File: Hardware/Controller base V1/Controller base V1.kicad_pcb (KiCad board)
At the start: 2 copper layers, 30 x 50 mm, 29 parts, among them J1 USB_C_Receptacle_USB2.0_16P, J7 Conn_02x10_Counter_Clockwise, J8 Conn_02x10_Counter_Clockwise, SW4 SW_Push, U1 AZ1117CH-3.3TRG1, U2 ESP32-S3-WROOM-1U-N4

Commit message: update
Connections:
- J8 pad 16: GND -> GPIO39
- J8 pad 18: GND -> GPIO40
- U2 pad 32: unconnected-(U2-IO39-Pad32) -> GPIO39
- U2 pad 33: unconnected-(U2-IO40-Pad33) -> GPIO40
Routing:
- net GPIO40: track 0.00 -> 15.6 mm, vias 0 -> 1
- net GPIO39: track 0.00 -> 13.3 mm, vias 0 -> 1
- net GND: track 75.0 -> 69.2 mm
- net GPIO16: track 12.8 -> 14.0 mm
- net GPIO15: track 16.2 -> 15.2 mm
- net GPIO6: track 12.1 -> 12.7 mm
- net GPIO5: track 13.4 -> 13.9 mm

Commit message: added test points
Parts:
- added 3V3: TestPoint, MCU_Controller:TestPoint_Pad_D1.0mm, F.Cu at (135.8, 77.1)
- added Gnd1: TestPoint, MCU_Controller:TestPoint_Pad_D1.0mm, F.Cu at (132.0, 108.8)
- added VBUS: TestPoint, MCU_Controller:TestPoint_Pad_D1.0mm, F.Cu at (149.3, 73.5)
- renumbered TP4 to D+1, TP3 to D-1, J7 to J3, J8 to J4, TP1 to RX0, SW4 to SW1, TP2 to TX0
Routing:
- net GND: track 69.2 -> 81.4 mm
- net VBUS: track 24.4 -> 27.7 mm
- net VCC_3V3: track 59.5 -> 62.2 mm

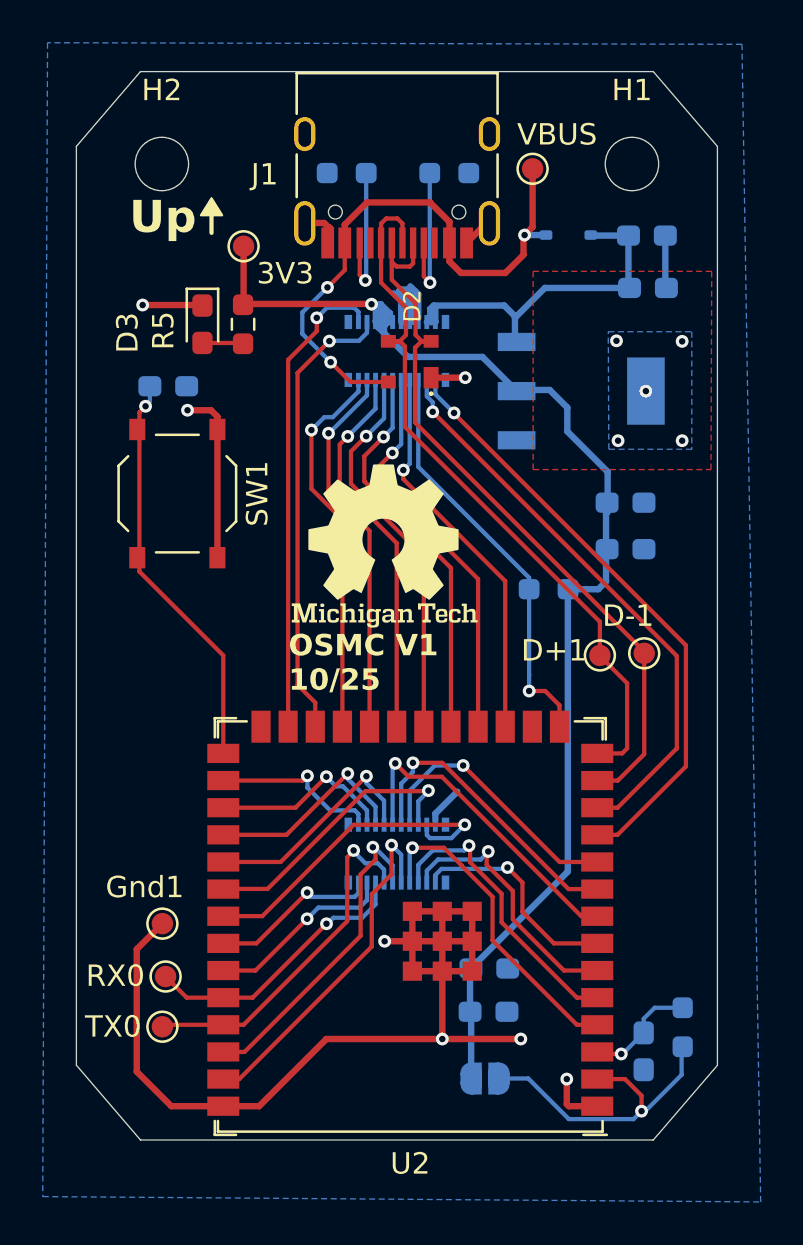
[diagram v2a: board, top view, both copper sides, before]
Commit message: trace update
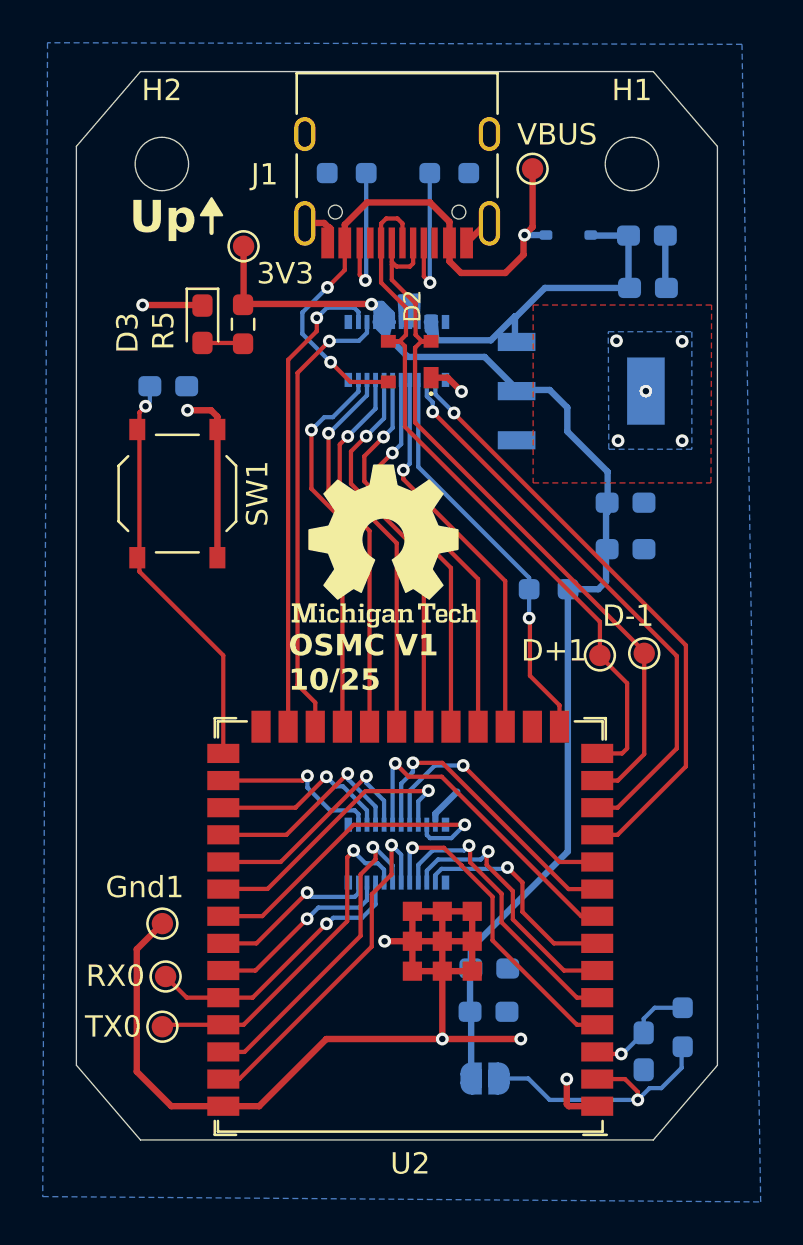
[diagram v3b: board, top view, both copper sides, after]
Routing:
- net GND: track 81.4 -> 72.2 mm
- net ESP_3.3V: track 15.3 -> 13.7 mm
- net VCC_3V3: track 62.2 -> 60.7 mm
- net VCC_5V: track 17.9 -> 16.9 mm

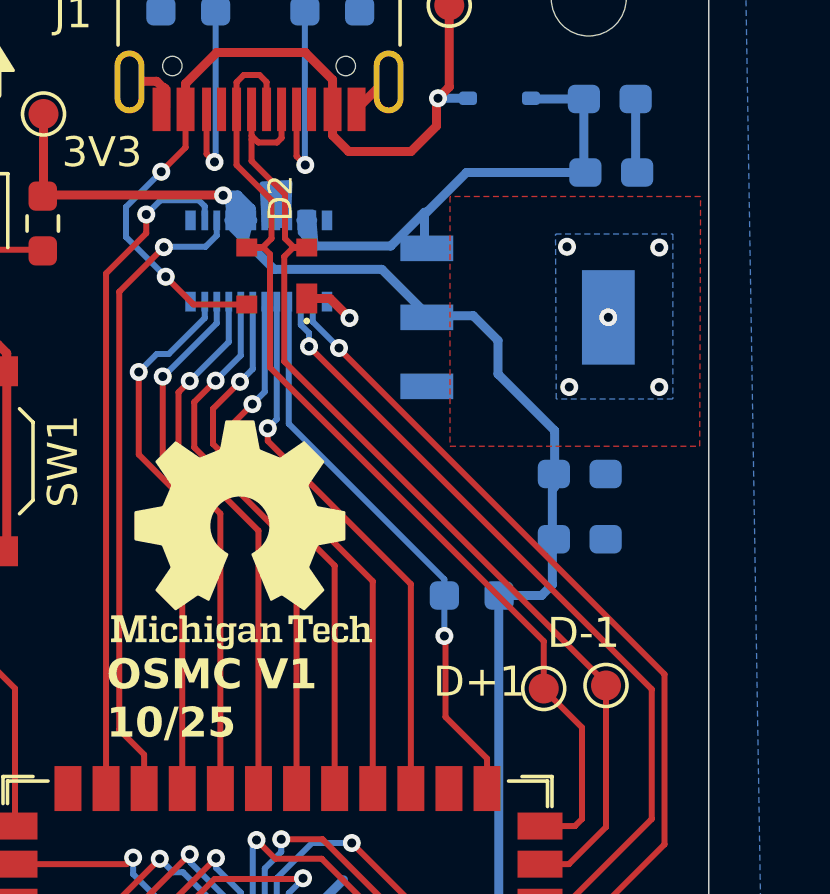
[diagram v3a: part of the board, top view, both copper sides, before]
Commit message: updated traces and labels
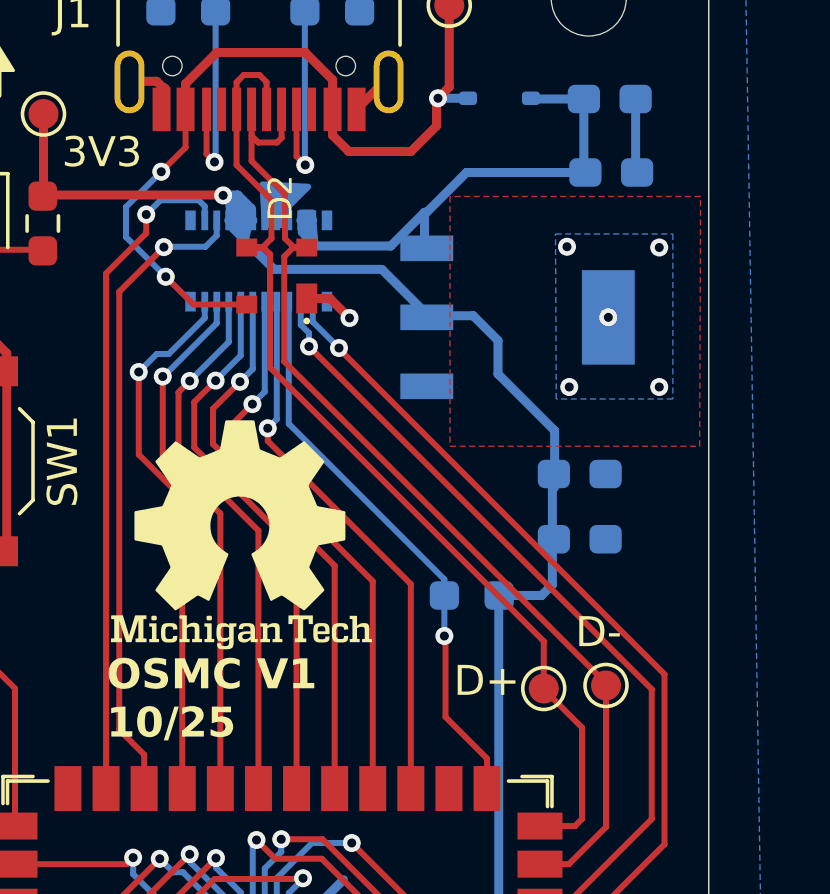
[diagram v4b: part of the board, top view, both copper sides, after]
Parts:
- renumbered D+1 to D+, D-1 to D-
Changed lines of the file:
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@@
 		(descr "SMD pad as test Point, diameter 1.0mm")
 		(tags "test point SMD pad")
-		(property "Reference" "D-1"
-			(at -0.75 -1.75 0)
+		(property "Reference" "D-"
+			(at -0.25 -1.775 0)
 			(layer "F.SilkS")
 			(effects
@@
 		(descr "SMD pad as test Point, diameter 1.0mm")
 		(tags "test point SMD pad")
-		(property "Reference" "D+1"
-			(at -2.15 -0.225 0)
+		(property "Reference" "D+"
+			(at -1.9 -0.25 0)
 			(layer "F.SilkS")
 			(effects
@@
 	(gr_poly
 		(pts
-			(xy 143.925 80.775) (xy 143.15 80.775) (xy 143.074522 79.421178) (xy 143.975 79.375) (xy 143.925 80.6)
+			(xy 143.925 80.775) (xy 143.15 80.775) (xy 143.074522 79.421178) (xy 144.6 79.5) (xy 143.925 80.175)
 		)
 		(stroke
